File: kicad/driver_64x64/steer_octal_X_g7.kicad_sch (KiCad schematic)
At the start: 66 parts

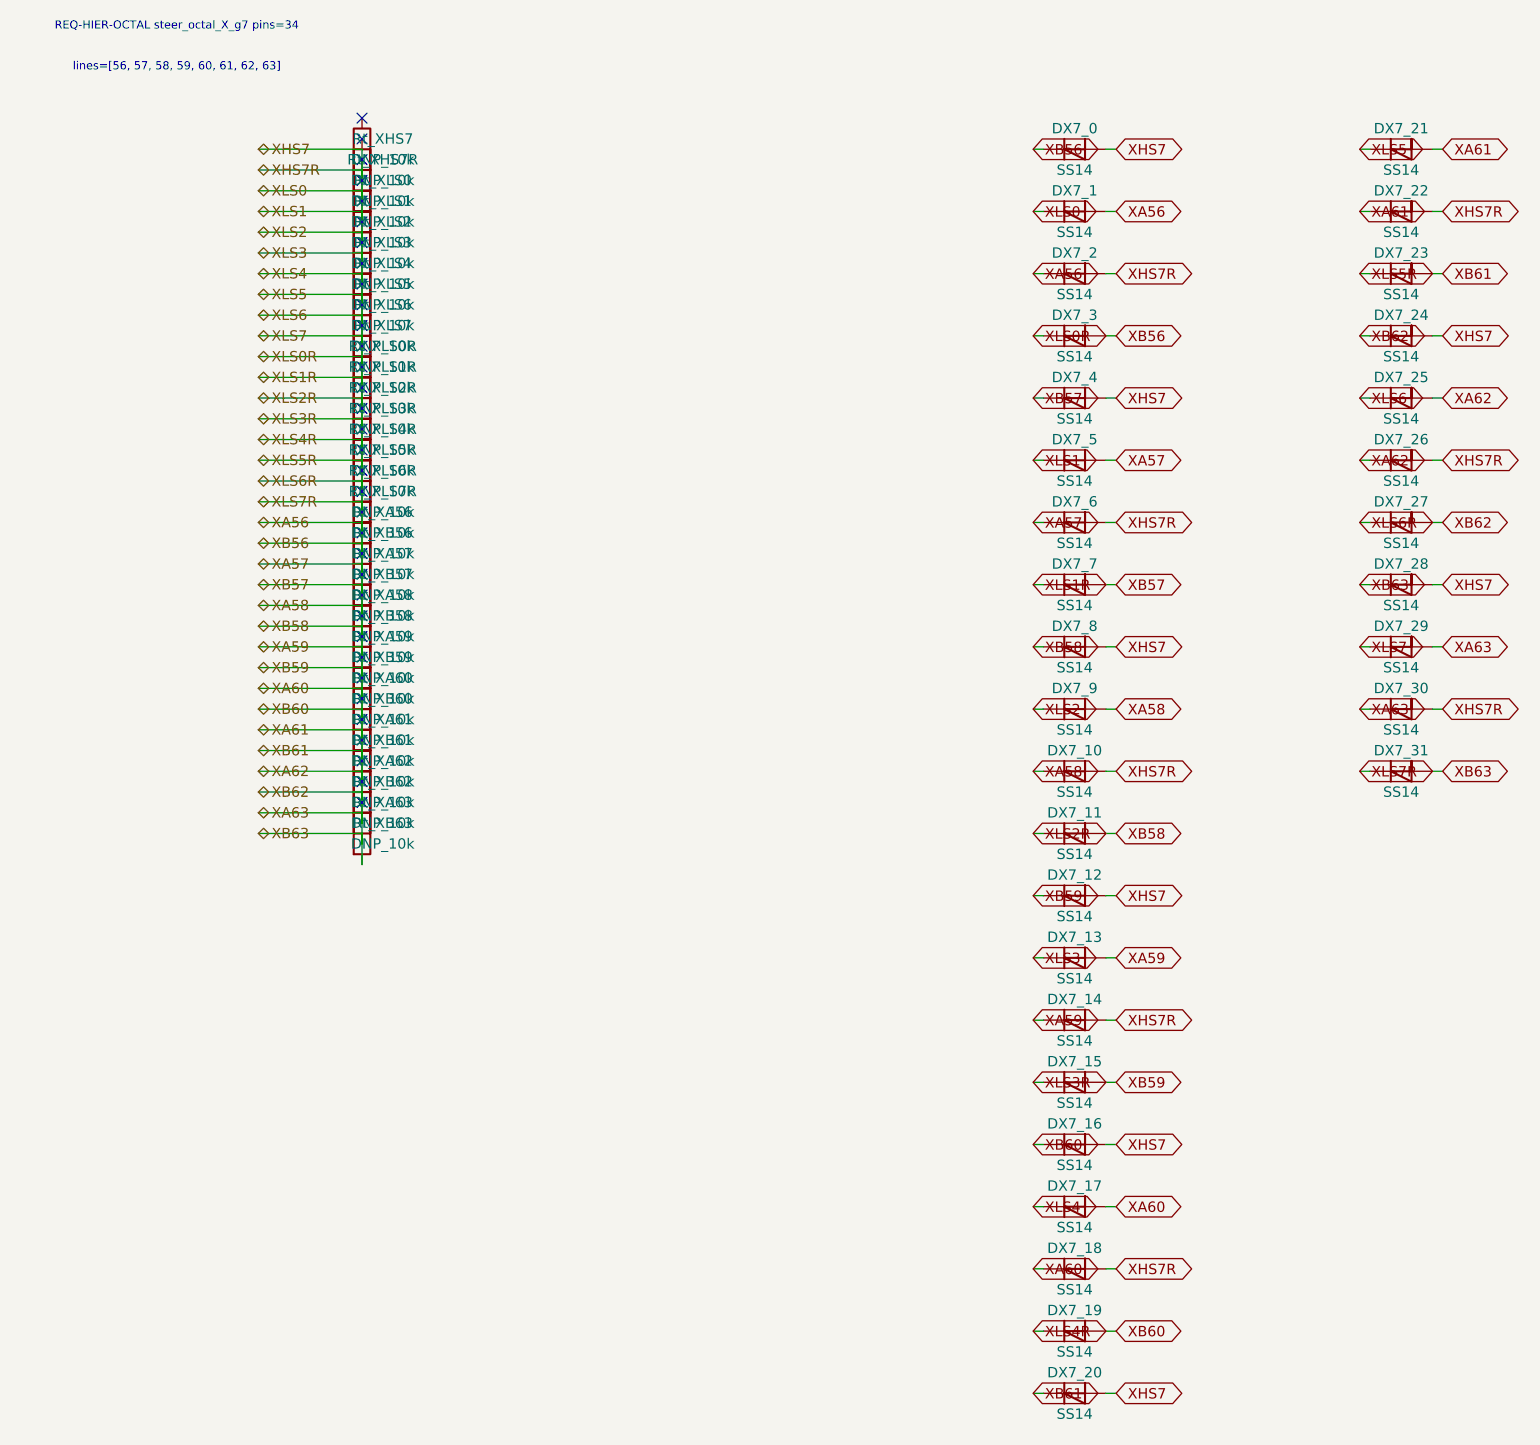
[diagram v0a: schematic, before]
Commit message: logical seperation into host and multiple decode/drive/steering boards
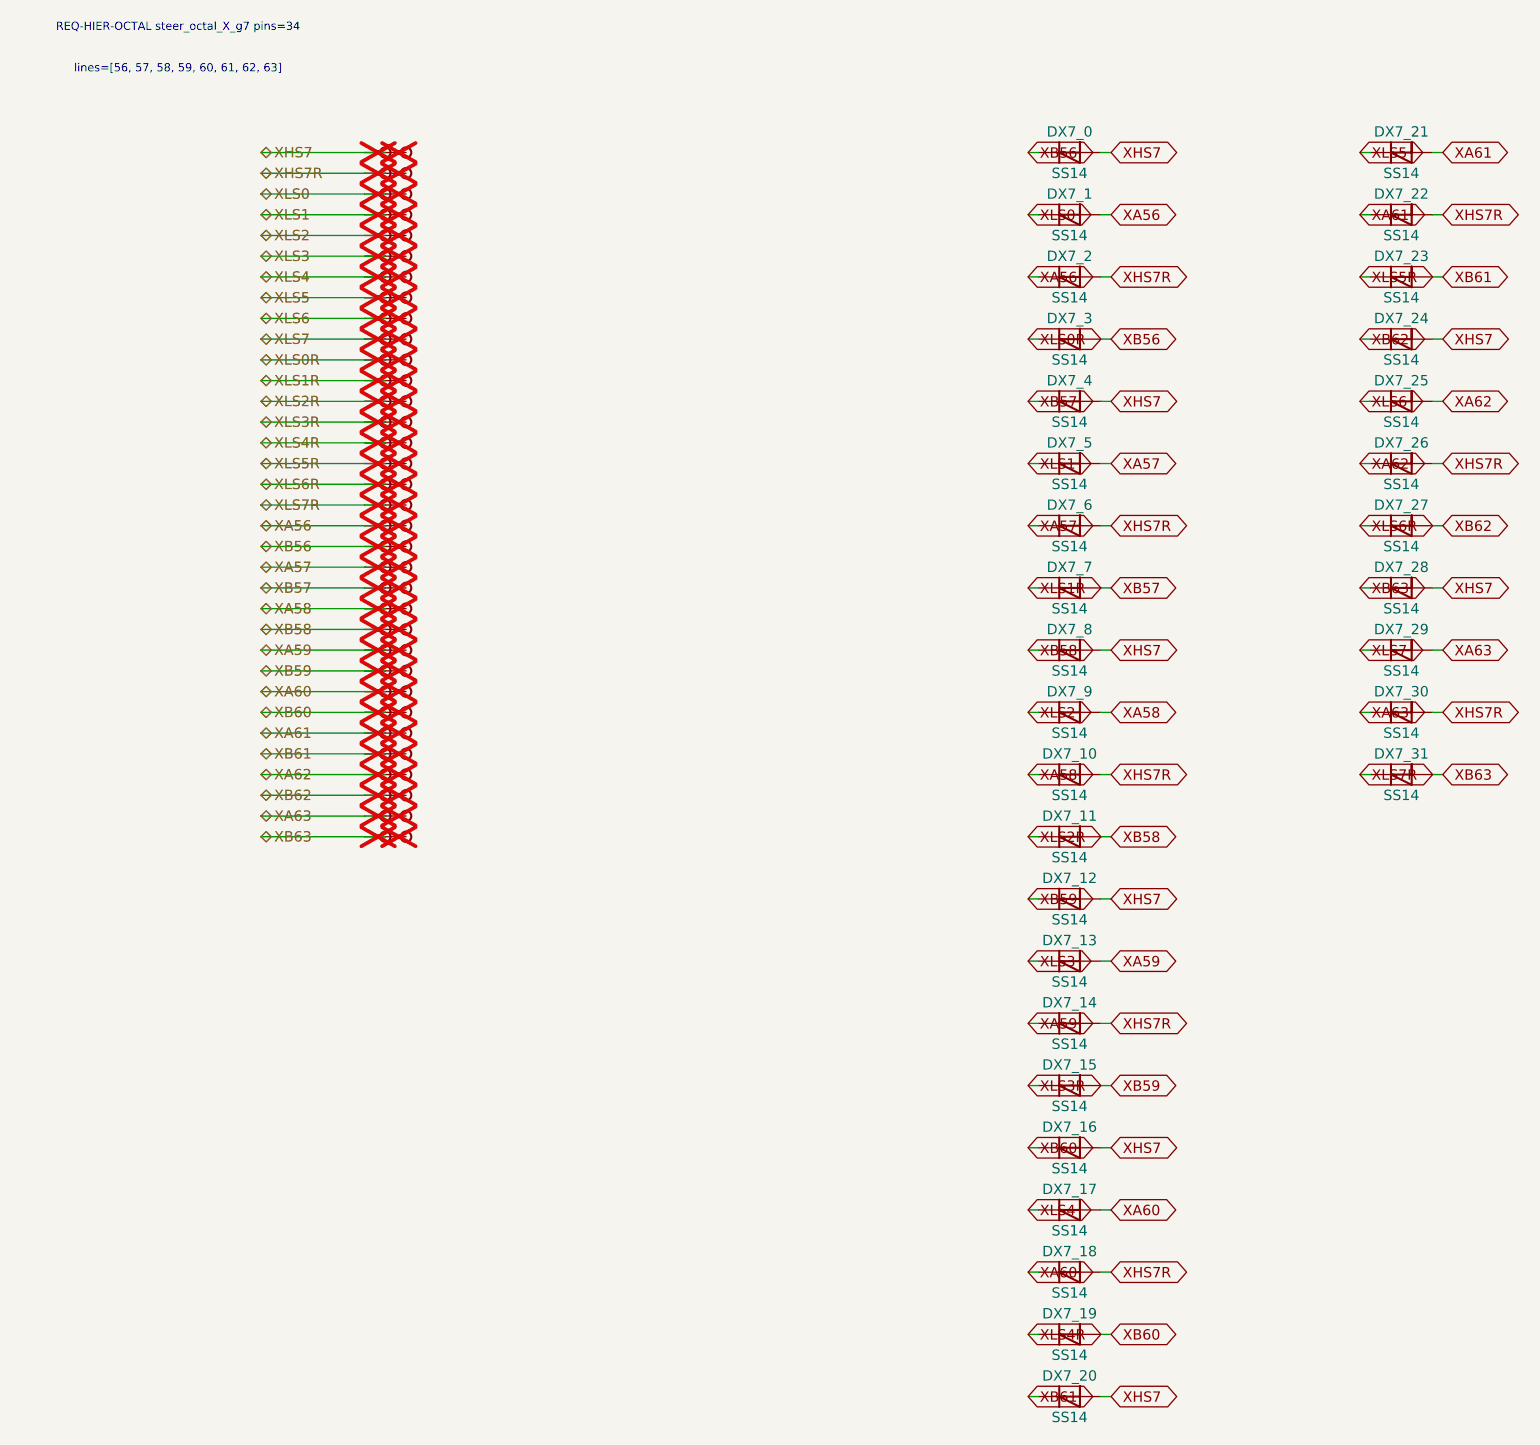
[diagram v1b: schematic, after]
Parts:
- removed Rt_XA56, Rt_XA57, Rt_XA58, Rt_XA59, Rt_XA60, Rt_XA61, Rt_XA62, Rt_XA63, Rt_XB56, Rt_XB57, Rt_XB58, Rt_XB59, Rt_XB60, Rt_XB61, Rt_XB62, Rt_XB63, Rt_XHS7, Rt_XHS7R, Rt_XLS0, Rt_XLS0R, Rt_XLS1, Rt_XLS1R, Rt_XLS2, Rt_XLS2R, Rt_XLS3, Rt_XLS3R, Rt_XLS4, Rt_XLS4R, Rt_XLS5, Rt_XLS5R, Rt_XLS6, Rt_XLS6R, Rt_XLS7, Rt_XLS7R: DNP_10k, symbol Device:R
- added TP_XA56, TP_XA56b, TP_XA57, TP_XA57b, TP_XA58, TP_XA58b, TP_XA59, TP_XA59b, TP_XA60, TP_XA60b, TP_XA61, TP_XA61b, TP_XA62, TP_XA62b, TP_XA63, TP_XA63b, TP_XB56, TP_XB56b, TP_XB57, TP_XB57b, TP_XB58, TP_XB58b, TP_XB59, TP_XB59b, TP_XB60, TP_XB60b, TP_XB61, TP_XB61b, TP_XB62, TP_XB62b, TP_XB63, TP_XB63b, TP_XHS7, TP_XHS7R, TP_XHS7Rb, TP_XHS7b, TP_XLS0, TP_XLS0R, TP_XLS0Rb, TP_XLS0b, TP_XLS1, TP_XLS1R, TP_XLS1Rb, TP_XLS1b, TP_XLS2, TP_XLS2R, TP_XLS2Rb, TP_XLS2b, TP_XLS3, TP_XLS3R, TP_XLS3Rb, TP_XLS3b, TP_XLS4, TP_XLS4R, TP_XLS4Rb, TP_XLS4b, TP_XLS5, TP_XLS5R, TP_XLS5Rb, TP_XLS5b, TP_XLS6, TP_XLS6R, TP_XLS6Rb, TP_XLS6b, TP_XLS7, TP_XLS7R, TP_XLS7Rb, TP_XLS7b: Stub, symbol CMR:Stub
- DX7_0, DX7_1, DX7_10, DX7_11, DX7_12, DX7_13, DX7_14, DX7_15, DX7_16, DX7_17, DX7_18, DX7_19, DX7_2, DX7_20, DX7_21, DX7_22, DX7_23, DX7_24, DX7_25, DX7_26, DX7_27, DX7_28, DX7_29, DX7_3, DX7_30, DX7_31, DX7_4, DX7_5, DX7_6, DX7_7, DX7_8, DX7_9: symbol Device:D_Schottky -> CMR:D_Schottky
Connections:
- net XA56: now also TP_XA56.1, TP_XA56b.1; no longer DX7_0.1 (K), DX7_0.2 (A), DX7_1.1 (K), DX7_10.1 (K), DX7_10.2 (A), DX7_11.1 (K), DX7_11.2 (A), DX7_12.1 (K), DX7_12.2 (A), DX7_13.1 (K), DX7_13.2 (A), DX7_14.1 (K), DX7_14.2 (A), DX7_15.1 (K), DX7_15.2 (A), DX7_16.1 (K), DX7_16.2 (A), DX7_17.1 (K), DX7_17.2 (A), DX7_18.1 (K), DX7_18.2 (A), DX7_19.1 (K), DX7_19.2 (A), DX7_2.2 (A), DX7_20.1 (K), DX7_20.2 (A), DX7_21.1 (K), DX7_21.2 (A), DX7_22.1 (K), DX7_22.2 (A), DX7_23.1 (K), DX7_23.2 (A), DX7_24.1 (K), DX7_24.2 (A), DX7_25.1 (K), DX7_25.2 (A), DX7_26.1 (K), DX7_26.2 (A), DX7_27.1 (K), DX7_27.2 (A), DX7_28.1 (K), DX7_28.2 (A), DX7_29.1 (K), DX7_29.2 (A), DX7_3.1 (K), DX7_3.2 (A), DX7_30.1 (K), DX7_30.2 (A), DX7_31.1 (K), DX7_31.2 (A), DX7_4.1 (K), DX7_4.2 (A), DX7_5.1 (K), DX7_5.2 (A), DX7_6.1 (K), DX7_6.2 (A), DX7_7.1 (K), DX7_7.2 (A), DX7_8.1 (K), DX7_8.2 (A), DX7_9.1 (K), DX7_9.2 (A)
- new net XA57: DX7_5.2 (A), DX7_6.1 (K), TP_XA57.1, TP_XA57b.1
- new net XA58: DX7_10.1 (K), DX7_9.2 (A), TP_XA58.1, TP_XA58b.1
- new net XA59: DX7_13.2 (A), DX7_14.1 (K), TP_XA59.1, TP_XA59b.1
- new net XA60: DX7_17.2 (A), DX7_18.1 (K), TP_XA60.1, TP_XA60b.1
- new net XA61: DX7_21.2 (A), DX7_22.1 (K), TP_XA61.1, TP_XA61b.1
- new net XA62: DX7_25.2 (A), DX7_26.1 (K), TP_XA62.1, TP_XA62b.1
- new net XA63: DX7_29.2 (A), DX7_30.1 (K), TP_XA63.1, TP_XA63b.1
- new net XB56: DX7_0.1 (K), DX7_3.2 (A), TP_XB56.1, TP_XB56b.1
- new net XB57: DX7_4.1 (K), DX7_7.2 (A), TP_XB57.1, TP_XB57b.1
- new net XB58: DX7_11.2 (A), DX7_8.1 (K), TP_XB58.1, TP_XB58b.1
- new net XB59: DX7_12.1 (K), DX7_15.2 (A), TP_XB59.1, TP_XB59b.1
- new net XB60: DX7_16.1 (K), DX7_19.2 (A), TP_XB60.1, TP_XB60b.1
- new net XB61: DX7_20.1 (K), DX7_23.2 (A), TP_XB61.1, TP_XB61b.1
- new net XB62: DX7_24.1 (K), DX7_27.2 (A), TP_XB62.1, TP_XB62b.1
- new net XB63: DX7_28.1 (K), DX7_31.2 (A), TP_XB63.1, TP_XB63b.1
- new net XHS7: DX7_0.2 (A), DX7_12.2 (A), DX7_16.2 (A), DX7_20.2 (A), DX7_24.2 (A), DX7_28.2 (A), DX7_4.2 (A), DX7_8.2 (A), TP_XHS7.1, TP_XHS7b.1
- new net XHS7R: DX7_10.2 (A), DX7_14.2 (A), DX7_18.2 (A), DX7_2.2 (A), DX7_22.2 (A), DX7_26.2 (A), DX7_30.2 (A), DX7_6.2 (A), TP_XHS7R.1, TP_XHS7Rb.1
- new net XLS0: DX7_1.1 (K), TP_XLS0.1, TP_XLS0b.1
- new net XLS0R: DX7_3.1 (K), TP_XLS0R.1, TP_XLS0Rb.1
- new net XLS1: DX7_5.1 (K), TP_XLS1.1, TP_XLS1b.1
- new net XLS1R: DX7_7.1 (K), TP_XLS1R.1, TP_XLS1Rb.1
- new net XLS2: DX7_9.1 (K), TP_XLS2.1, TP_XLS2b.1
- new net XLS2R: DX7_11.1 (K), TP_XLS2R.1, TP_XLS2Rb.1
- new net XLS3: DX7_13.1 (K), TP_XLS3.1, TP_XLS3b.1
- new net XLS3R: DX7_15.1 (K), TP_XLS3R.1, TP_XLS3Rb.1
- new net XLS4: DX7_17.1 (K), TP_XLS4.1, TP_XLS4b.1
- new net XLS4R: DX7_19.1 (K), TP_XLS4R.1, TP_XLS4Rb.1
- new net XLS5: DX7_21.1 (K), TP_XLS5.1, TP_XLS5b.1
- new net XLS5R: DX7_23.1 (K), TP_XLS5R.1, TP_XLS5Rb.1
- new net XLS6: DX7_25.1 (K), TP_XLS6.1, TP_XLS6b.1
- new net XLS6R: DX7_27.1 (K), TP_XLS6R.1, TP_XLS6Rb.1
- new net XLS7: DX7_29.1 (K), TP_XLS7.1, TP_XLS7b.1
- new net XLS7R: DX7_31.1 (K), TP_XLS7R.1, TP_XLS7Rb.1
- no-connect marks 34 -> 0
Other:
- moved on the sheet: DX7_0, DX7_1, DX7_10, DX7_11, DX7_12, DX7_13, DX7_14, DX7_15, DX7_16, DX7_17, DX7_18, DX7_19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
